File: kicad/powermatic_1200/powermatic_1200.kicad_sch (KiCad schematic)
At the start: 27 parts, among them J1 T4171310004-001, J2 3PH-4W-PLUG, K1 HC3096N-52-900-24, K2 HMC-9B30-11-DS, K3 HMC-9B30-11-DS, K4 HMC-9B30-11-DS, K5 HMC-9B30-11-DS, K6 HMC-9B30-11-DS, M1 PWRM1200-MOTOR, Q1 FAZ-D4/2-NA-L, SW1 222102

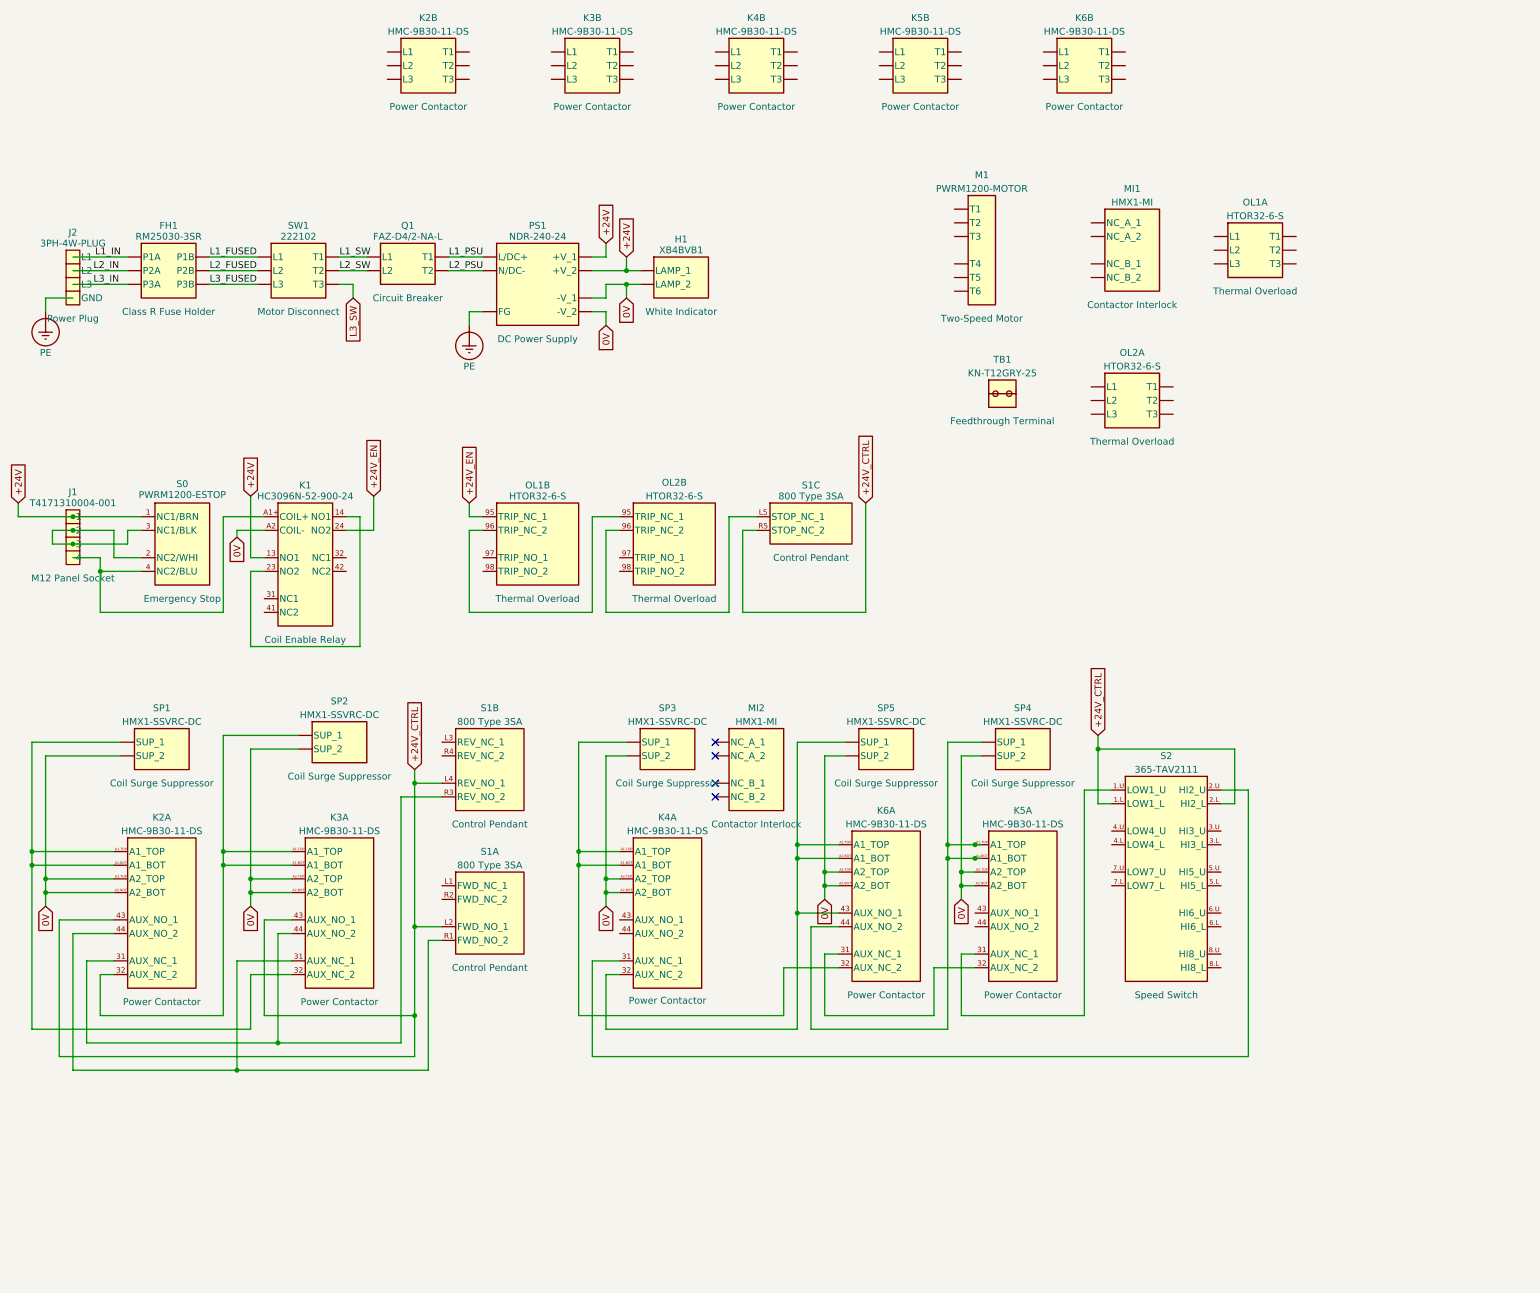
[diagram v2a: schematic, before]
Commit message: added duct and din
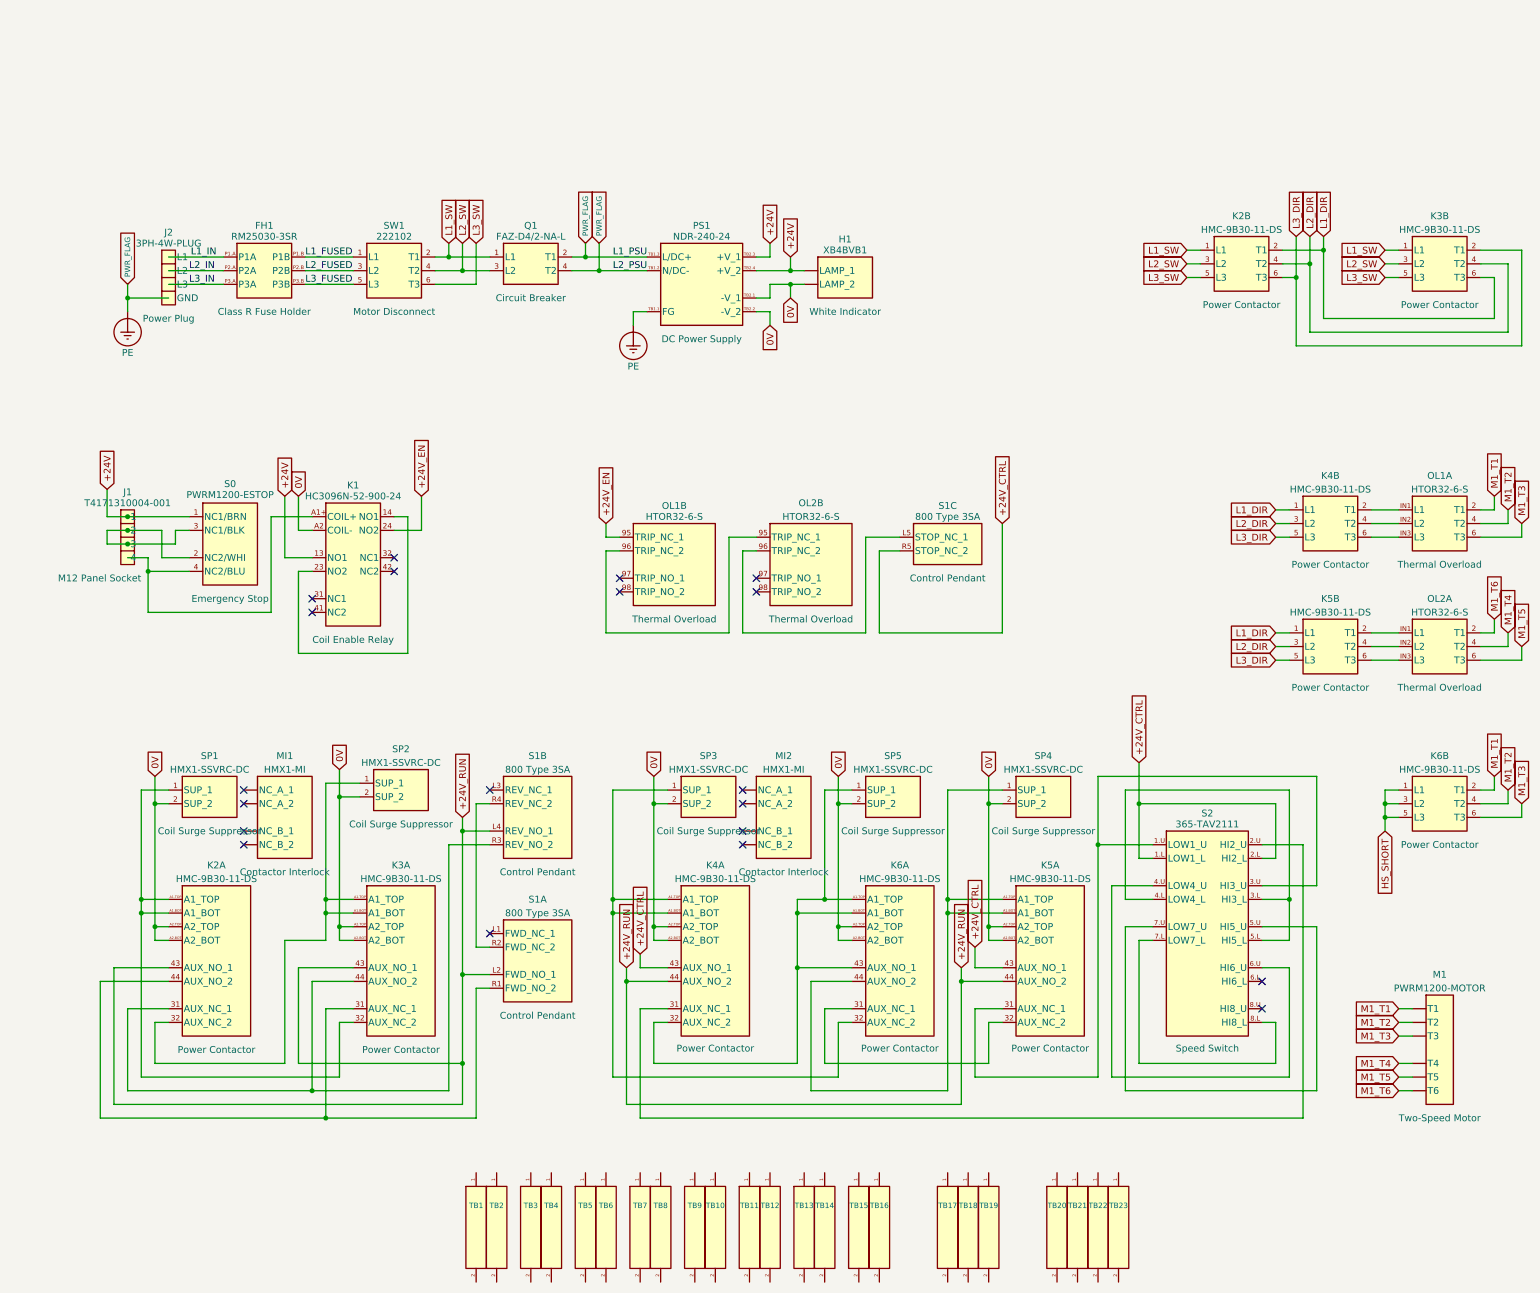
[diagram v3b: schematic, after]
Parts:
- added TB10, TB11, TB12, TB13, TB14, TB15, TB16, TB17, TB18, TB19, TB2, TB20, TB21, TB22, TB23, TB3, TB4, TB5, TB6, TB7, TB8, TB9: KN-T12GRY-25, Controls:KN-T12GRY-25_Front, symbol Controls:KN-T12GRY-25
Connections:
- net +24V_CTRL: now also K4.43 (AUX_NO_1), K5.43 (AUX_NO_1); no longer K2.43 (AUX_NO_1), K3.43 (AUX_NO_1), S1.L2 (FWD_NO_1), S1.L4 (REV_NO_1)
- net L1_SW: now also K2.1 (L1), K3.1 (L1)
- net L2_SW: now also K2.3 (L2), K3.3 (L2)
- net L3_SW: now also K2.5 (L3), K3.5 (L3)
- net at K5.31 (AUX_NC_1), S2.1.U (LOW1_U): now also S2.3.U (HI3_U)
- net +24V_RUN: now reaches K5.44 (AUX_NO_2)
- net +24V_RUN: now also K2.43 (AUX_NO_1), K3.43 (AUX_NO_1), K4.44 (AUX_NO_2), S1.L2 (FWD_NO_1), S1.L4 (REV_NO_1)
- net L1_DIR: now reaches K2.2 (T1)
- net L1_DIR: now also K3.6 (T3), K4.1 (L1), K5.1 (L1)
- net L2_DIR: now reaches K2.4 (T2)
- net L2_DIR: now also K3.4 (T2), K4.3 (L2), K5.3 (L2)
- net L3_DIR: now reaches K2.6 (T3)
- net L3_DIR: now also K3.2 (T1), K4.5 (L3), K5.5 (L3)
- net at S1.R2 (FWD_NC_2): now also S1.R4 (REV_NC_2)
- net M1_T6: now reaches OL2.2 (T1)
- net M1_T6: now also M1.T6
- net M1_T4: now reaches OL2.4 (T2)
- net M1_T4: now also M1.T4
- net M1_T5: now reaches OL2.6 (T3)
- net M1_T5: now also M1.T5
- net at OL2.IN1 (L1): now also K5.2 (T1)
- net at OL2.IN2 (L2): now also K5.4 (T2)
- net at OL2.IN3 (L3): now also K5.6 (T3)
- net M1_T1: now reaches M1.T1
- net M1_T1: now also K6.2 (T1), OL1.2 (T1)
- net M1_T2: now reaches M1.T2
- net M1_T2: now also K6.4 (T2), OL1.4 (T2)
- net M1_T3: now reaches M1.T3
- net M1_T3: now also K6.6 (T3), OL1.6 (T3)
- net HS_SHORT: now reaches K6.1 (L1)
- net HS_SHORT: now also K6.3 (L2), K6.5 (L3)
- net at OL1.IN1 (L1): now also K4.2 (T1)
- net at OL1.IN2 (L2): now also K4.4 (T2)
- net at OL1.IN3 (L3): now also K4.6 (T3)
- net at S2.3.L (HI3_L): now also S2.4.L (LOW4_L), S2.5.L (HI5_L)
- net at S2.4.U (LOW4_U): now also S2.6.U (HI6_U)
- net at S2.5.U (HI5_U): now also S2.7.U (LOW7_U)
- net at S2.7.L (LOW7_L): now also S2.8.L (HI8_L)
- no-connect marks 4 -> 20
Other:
- moved on the sheet: H1, J1, J2, K1, K2A, K3A, K4A, K5A, K6A, M1, MI1, MI2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

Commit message: panel layout
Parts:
- added TB22, TB25, TB28, TB31, TB34, TB35: KN-G12SP-10, Controls:KN-G12SP-10_Front, symbol Controls:KN-G12SP-10
- added TB26, TB27, TB29, TB30, TB32, TB33: KN-T12GRY-25, Controls:KN-T12GRY-25_Front, symbol Controls:KN-T12GRY-25
- K2: renamed from K1; footprint (none) -> Controls:HC3096N-52-900-24_Front; Package (none) -> DIN-RAIL
- renumbered K2 to K1, K6 to K5, K5 to K6, S0 to S1, S1 to S2, S2 to S3, SP5 to SP4, SP4 to SP5, TB15 to TB10, TB6 to TB11, TB16 to TB12, TB7 to TB13, TB17 to TB14, TB8 to TB15, TB18 to TB16, TB9 to TB17, TB22 to TB18, TB10 to TB19, TB11 to TB2, TB23 to TB20, TB20 to TB21, TB21 to TB23, TB19 to TB24, TB2 to TB3, TB12 to TB4, TB3 to TB5, TB13 to TB6, TB4 to TB7, TB14 to TB8, TB5 to TB9
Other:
- moved on the sheet: TB10, TB12, TB14, TB16, TB18, TB2, TB20, TB21, TB23, TB24, TB4, TB6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

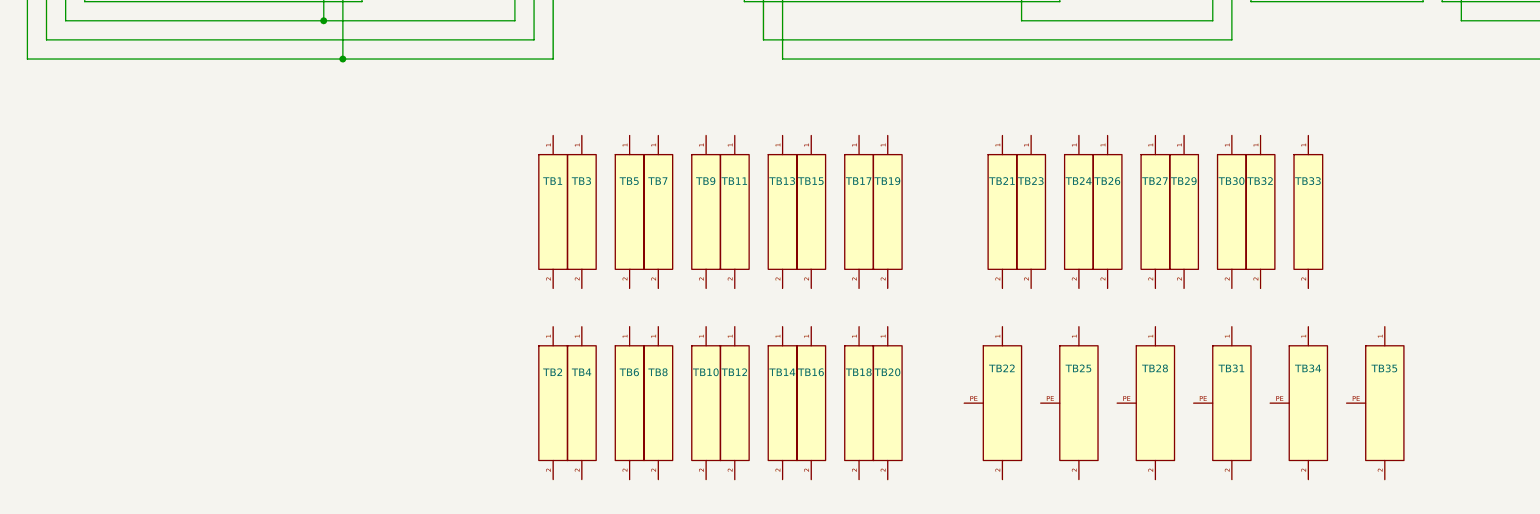
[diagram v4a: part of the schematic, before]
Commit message: Update enclosure BOM, footprint artwork, and assembly model alignment
Preserve detailed drawings on F.Fab, use simplified F.SilkS outlines and F.Adhes fills, and align contactor accessories to the nominal Fusion assembly. Include current schematic and terminal placement edits, model verification tools, and review artifacts.

Record reconciliation with the shared parts rail export. KiCad loads all 58 board footprints, model checks pass, and the schematic netlist exports successfully. Nominal assembly alignment is not a collision-free fit approval.
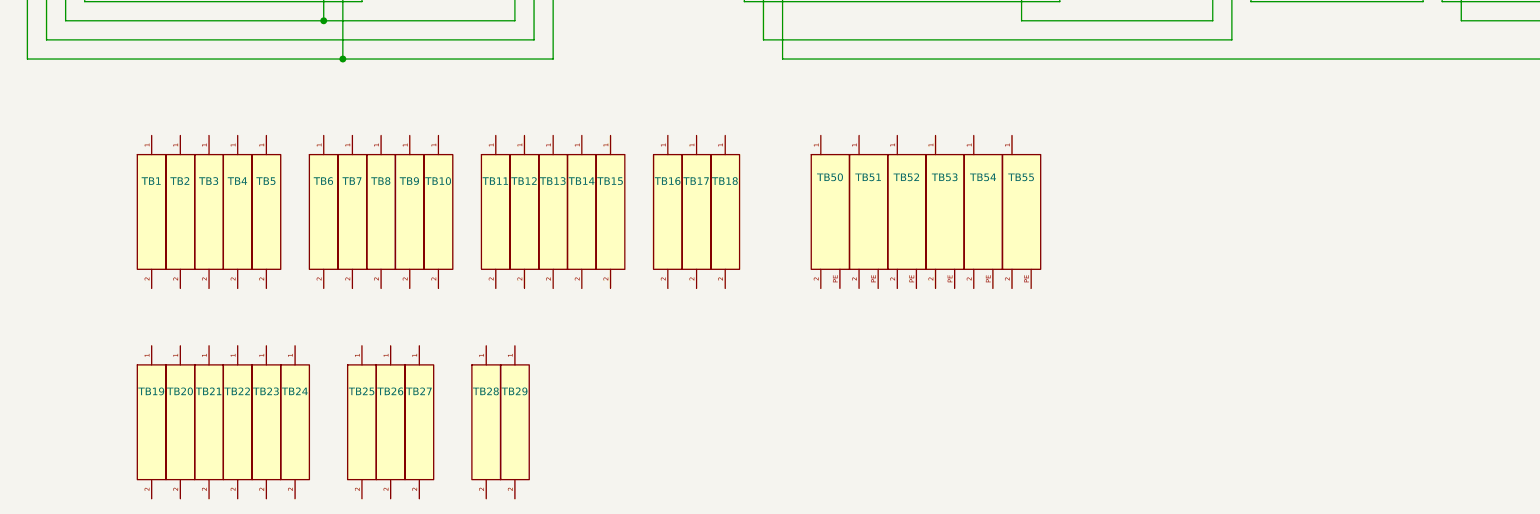
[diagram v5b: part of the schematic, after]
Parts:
- renumbered TB23 to TB22, TB24 to TB23, TB26 to TB24, TB27 to TB25, TB29 to TB26, TB30 to TB27, TB32 to TB28, TB33 to TB29, TB22 to TB50, TB25 to TB51, TB28 to TB52, TB31 to TB53, TB34 to TB54, TB35 to TB55
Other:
- moved on the sheet: TB1, TB10, TB11, TB12, TB13, TB14, TB15, TB16, TB17, TB18, TB19, TB2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

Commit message: finalized panel layout
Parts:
- removed TB10, TB11, TB17, TB19, TB8: KN-T12GRY-25, Controls:KN-T12GRY-25_Front, symbol Controls:KN-T12GRY-25
- removed TB50, TB51, TB52: KN-G12SP-10, Controls:KN-G12SP-10_Front, symbol Controls:KN-G12SP-10
- added J3: BNSPDX-23-W, Controls:BNSPDX-23-W_BottomWall, symbol Controls:BNSPDX-23-W
- added J4: BSPDX-23-W, Controls:BSPDX-23-W_BottomWall, symbol Controls:BSPDX-23-W
- added J5: BSPBX-22-W, Controls:BSPBX-22-W_BottomWall, symbol Controls:BSPBX-22-W
- added TB1, TB60, TB62, TB64: KN-T12GRY-25, Controls:KN-T12GRY-25_Front, symbol Controls:KN-T12GRY-25
- renumbered K3 to K2, K2 to K3, TB1 to TB10, TB3 to TB11, TB5 to TB12, TB7 to TB13, TB9 to TB14, TB13 to TB2, TB18 to TB20, TB20 to TB21, TB2 to TB22, TB4 to TB23, TB6 to TB24, TB15 to TB3, TB16 to TB30, TB14 to TB31, TB12 to TB32, TB23 to TB40, TB21 to TB41, TB22 to TB42, TB55 to TB50, TB54 to TB51, TB53 to TB52, TB24 to TB61, TB25 to TB63, TB26 to TB65, TB27 to TB66, TB28 to TB67, TB29 to TB68
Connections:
- net +24V: now also TB2.1 (TERM), TB2.2 (TERM), TB3.1 (TERM), TB3.2 (TERM), TB1.1 (TERM), TB1.2 (TERM)
- net +24V_CTRL: now also TB20.1 (TERM), TB20.2 (TERM), TB21.1 (TERM), TB21.2 (TERM), J5.1 (+24V_CTRL)
- net +24V_RUN: now also TB22.1 (TERM), TB22.2 (TERM), TB23.1 (TERM), TB23.2 (TERM), TB24.1 (TERM), TB24.2 (TERM), J5.2 (+24V_RUN)
- net 0V: now also TB10.1 (TERM), TB10.2 (TERM), TB11.1 (TERM), TB11.2 (TERM), TB12.1 (TERM), TB12.2 (TERM), TB13.1 (TERM), TB13.2 (TERM), TB14.1 (TERM), TB14.2 (TERM)
- net L1_IN: now also TB40.1 (TERM), TB40.2 (TERM), J3.X (L1)
- net L2_IN: now also TB41.1 (TERM), TB41.2 (TERM), J3.Y (L2)
- net L3_IN: now also TB42.1 (TERM), TB42.2 (TERM), J3.Z (L3)
- net M1_T1: now also TB61.1 (TERM), TB61.2 (TERM), J4.T1, TB60.1 (TERM), TB60.2 (TERM)
- net M1_T2: now also TB63.1 (TERM), TB63.2 (TERM), J4.T2, TB62.1 (TERM), TB62.2 (TERM)
- net M1_T3: now also TB65.1 (TERM), TB65.2 (TERM), J4.T3, TB64.1 (TERM), TB64.2 (TERM)
- net M1_T4: now also TB66.1 (TERM), TB66.2 (TERM), J4.T4
- net M1_T5: now also TB67.1 (TERM), TB67.2 (TERM), J4.T5
- net M1_T6: now also TB68.1 (TERM), TB68.2 (TERM), J4.T6
- net PE: now also TB50.1 (TERM), TB50.2 (TERM), TB50.PE, TB51.1 (TERM), TB51.2 (TERM), TB51.PE, TB52.1 (TERM), TB52.2 (TERM), TB52.PE, J3.G (GND)
- net NC2/BLU: now reaches TB32.1 (TERM)
- net NC2/BLU: now also J1.4, K3.A1+ (COIL+), S1.4 (NC2/BLU), TB32.2 (TERM)
- net LOW_CMD: now reaches K6.31 (AUX_NC_1), S3.1.U (LOW1_U), S3.3.U (HI3_U)
- net LOW_CMD: now also J5.6 (LOW_CMD)
- net FWD_CMD: now reaches K1.44 (AUX_NO_2), K2.31 (AUX_NC_1), S2.R1 (FWD_NO_2)
- net FWD_CMD: now also J5.3 (FWD_CMD)
- net REV_CMD: now reaches K1.31 (AUX_NC_1), K2.44 (AUX_NO_2), S2.R3 (REV_NO_2)
- net REV_CMD: now also J5.4 (REV_CMD)
- net ESTOP_MID: now reaches J1.2, J1.3, S1.2 (NC2/WHI), S1.3 (NC1/BLK)
- net ESTOP_MID: now also TB30.1 (TERM), TB30.2 (TERM), TB31.1 (TERM), TB31.2 (TERM)
- net STOP_CHAIN: now reaches OL2.96 (TRIP_NC_2), S2.L5 (STOP_NC_1)
- net STOP_CHAIN: now also J5.5 (STOP_CHAIN)
- net HIGH_CMD: now reaches K4.31 (AUX_NC_1), S3.2.U (HI2_U)
- net HIGH_CMD: now also J5.7 (HIGH_CMD)
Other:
- note added: "3"
- note added: "4"
- note added: "5"
- note added: "BACKPLATE"
- note added: "DOOR"
- note added: "ENCLOSURE"
- note added: "H1.X1"
- note added: "H1.X2"
- note added: "J1.1"
- note added: "J2.G"
- note added: "J5.1"
- note added: "J5.2"
- note added: "K1.43"
- note added: "K1.A2_BOT"
- note added: "K2.43"
- note added: "K2.A2_BOT"
- note added: "K3.13"
- note added: "K3.A2"
- note added: "K4.43"
- note added: "K4.44"
- note added: "K4.A2_BOT"
- note added: "K5.2"
- note added: "K5.4"
- note added: "K5.6"
- note added: "K5.A2_BOT"
- note added: "K6.43"
- note added: "K6.44"
- note added: "K6.A2_BOT"
- note added: "M1.T1"
- note added: "M1.T2"
- note added: "M1.T3"
- note added: "M1.T4"
- note added: "M1.T5"
- note added: "M1.T6"
- note added: "MOTOR"
- note added: "OL1A.2"
- note added: "OL1A.4"
- note added: "OL1A.6"
- note added: "OL2A.2"
- note added: "OL2A.4"
- note added: "OL2A.6"
- note added: "PS1.TB1.1"
- note added: "PS1.TB2.1"
- note added: "PS1.TB2.3"
- note added: "SPARE"
- moved on the sheet: FH1, J1, K1A, K1B, K2A, K2B, K3, K4A, K4B, K5A, K5B, K6A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
